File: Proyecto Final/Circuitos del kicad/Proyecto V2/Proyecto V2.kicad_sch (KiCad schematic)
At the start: 40 parts, among them J1 12v, J2 I2C + LCD, J3 DS1307, J4 Encoder, J5 Conn_01x02, J6 Conn_01x02, J7 Conn_01x02, J8 Conn_01x05, J9 Conn_01x05, K1 RAYEX-L90, K2 RAYEX-L90, K3 RAYEX-L90, Q1 PN2222A, Q2 PN2222A, Q3 PN2222A, SW1 SW_Push, SW2 SW_Push, SW3 SW_Push, SW4 SW_Push, U1 LM7805, U3 ATmega328P-P, U4 NodeMCU1.0(ESP-12E), Y1 16MHz

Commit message: SEXOOO
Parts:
- removed J4: Encoder, Connector_PinSocket_2.54mm:PinSocket_1x05_P2.54mm_Vertical, symbol Connector_Generic:Conn_01x05
- removed J9: Conn_01x05, Connector_PinHeader_2.54mm:PinHeader_1x05_P2.54mm_Vertical, symbol Connector_Generic:Conn_01x05
- added J4: Conn_02x06_Odd_Even, Connector_PinHeader_2.54mm:PinHeader_2x06_P2.54mm_Vertical, symbol Connector_Generic:Conn_02x06_Odd_Even
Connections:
- net +5V: now also J4.1 (Pin_1), J4.2 (Pin_2)
- net GND: now also J4.11 (Pin_11), J4.12 (Pin_12)
- net at U3.23 (PC0): now also J4.8 (Pin_8)
- net at U3.24 (PC1): now also J4.6 (Pin_6)
- net at U3.4 (PD2): now also J4.3 (Pin_3)
- net at U3.5 (PD3): now also J4.5 (Pin_5)
- net at U3.6 (PD4): now also J4.7 (Pin_7)
- net at U3.11 (PD5): now also J4.9 (Pin_9)
- net at U3.25 (PC2): now also J4.4 (Pin_4)
- no-connect marks 34 -> 33

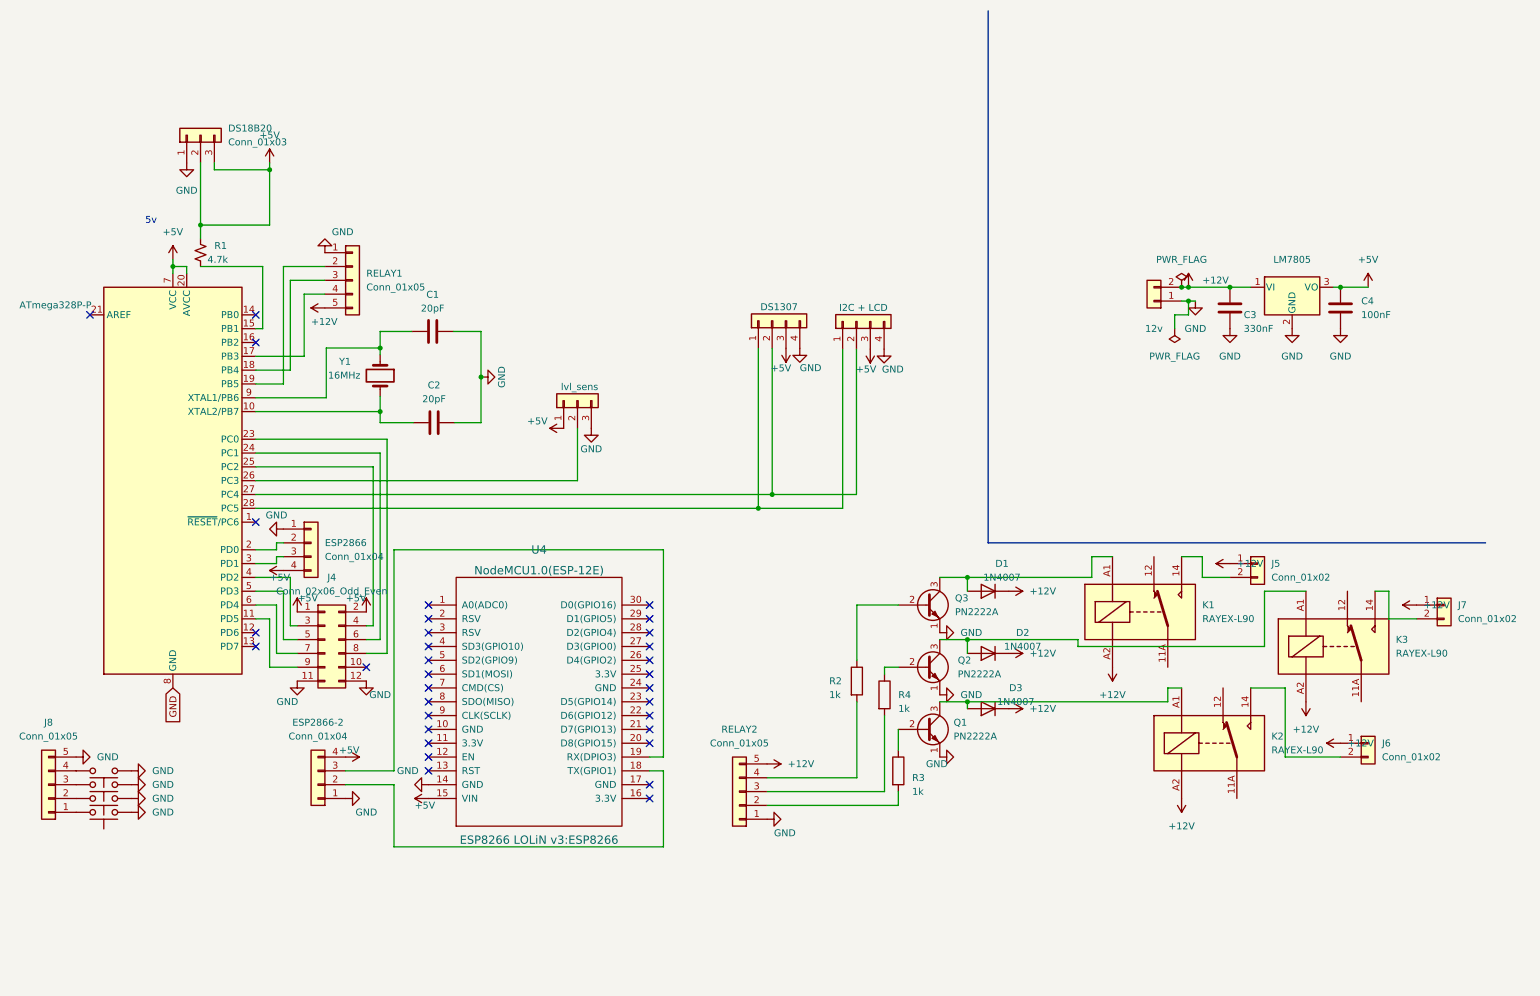
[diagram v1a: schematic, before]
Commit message: Resistencias pullup para pulsadores
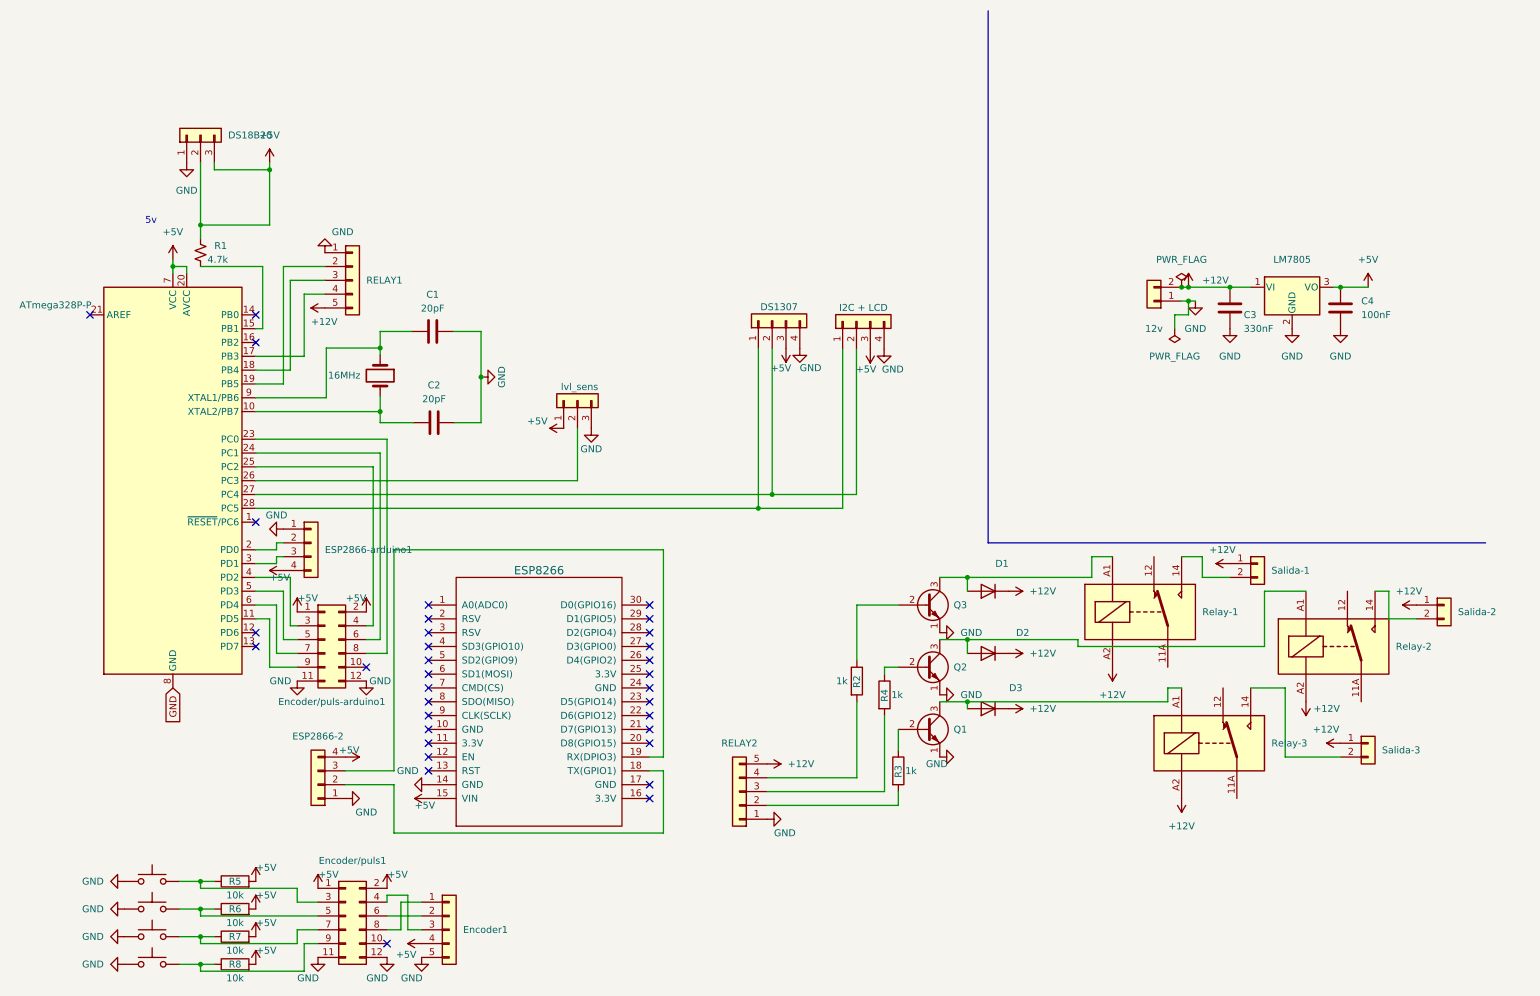
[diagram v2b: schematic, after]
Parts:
- removed J8: Conn_01x05, Connector_PinHeader_2.54mm:PinHeader_1x05_P2.54mm_Vertical, symbol Connector_Generic:Conn_01x05
- added Encoder/puls1: Conn_02x06_Odd_Even, Connector_PinHeader_2.54mm:PinHeader_2x06_P2.54mm_Vertical, symbol Connector_Generic:Conn_02x06_Odd_Even
- added Encoder1: Conn_01x05, Connector_PinSocket_2.54mm:PinSocket_1x05_P2.54mm_Vertical, symbol Connector_Generic:Conn_01x05
- added R5, R6, R7, R8: 10k, Resistor_THT:R_Axial_DIN0204_L3.6mm_D1.6mm_P5.08mm_Horizontal, symbol Device:R
- renumbered ESP2866 to ESP2866-arduino1, U4 to ESP8266, J4 to Encoder/puls-arduino1, K1 to Relay-1, K3 to Relay-2, K2 to Relay-3, J5 to Salida-1, J7 to Salida-2, J6 to Salida-3
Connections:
- net +5V: now also Encoder/puls1.1 (Pin_1), Encoder/puls1.2 (Pin_2), Encoder1.4 (Pin_4), R5.2, R6.2, R7.2, R8.2
- net GND: now also Encoder/puls1.11 (Pin_11), Encoder/puls1.12 (Pin_12), Encoder1.5 (Pin_5)
- net at SW2.2: now also Encoder/puls1.7 (Pin_7), R7.1
- net at SW3.2: now also Encoder/puls1.5 (Pin_5), R6.1
- net at SW1.2: now also Encoder/puls1.9 (Pin_9), R8.1
- net at SW4.2: now also Encoder/puls1.3 (Pin_3), R5.1
- new net: Encoder/puls1.4 (Pin_4), Encoder1.3 (Pin_3)
- new net: Encoder/puls1.6 (Pin_6), Encoder1.2 (Pin_2)
- new net: Encoder/puls1.8 (Pin_8), Encoder1.1 (Pin_1)
- no-connect marks 33 -> 34

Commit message: cambio bornera
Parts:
- Salida-1, Salida-2, Salida-3: footprint Connector_PinHeader_2.54mm:PinHeader_1x02_P2.54mm_Vertical -> TerminalBlock:TerminalBlock_bornier-2_P5.08mm
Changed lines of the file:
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@@
       (effects (font (size 1.27 1.27)) (justify left) hide)
     )
-    (property "Footprint" "Connector_PinHeader_2.54mm:PinHeader_1x02_P2.54mm_Vertical" (id 2) (at 264.16 146.05 0)
+    (property "Footprint" "TerminalBlock:TerminalBlock_bornier-2_P5.08mm" (id 2) (at 264.16 146.05 0)
       (effects (font (size 1.27 1.27)) hide)
     )
@@
       (effects (font (size 1.27 1.27)) (justify left) hide)
     )
-    (property "Footprint" "Connector_PinHeader_2.54mm:PinHeader_1x02_P2.54mm_Vertical" (id 2) (at 243.84 113.03 0)
+    (property "Footprint" "TerminalBlock:TerminalBlock_bornier-2_P5.08mm" (id 2) (at 243.84 113.03 0)
       (effects (font (size 1.27 1.27)) hide)
     )
@@
       (effects (font (size 1.27 1.27)) (justify left) hide)
     )
-    (property "Footprint" "Connector_PinHeader_2.54mm:PinHeader_1x02_P2.54mm_Vertical" (id 2) (at 278.13 120.65 0)
+    (property "Footprint" "TerminalBlock:TerminalBlock_bornier-2_P5.08mm" (id 2) (at 278.13 120.65 0)
       (effects (font (size 1.27 1.27)) hide)
     )
@@
     )
     (path "/1672224d-7982-4259-8536-1b27e643cf0c"
-      (reference "Salida-1") (unit 1) (value "Conn_01x02") (footprint "Connector_PinHeader_2.54mm:PinHeader_1x02_P2.54mm_Vertical")
+      (reference "Salida-1") (unit 1) (value "Conn_01x02") (footprint "TerminalBlock:TerminalBlock_bornier-2_P5.08mm")
     )
     (path "/2d58b5ac-6ee1-429c-aae4-017d7d7a7777"
-      (reference "Salida-2") (unit 1) (value "Conn_01x02") (footprint "Connector_PinHeader_2.54mm:PinHeader_1x02_P2.54mm_Vertical")
+      (reference "Salida-2") (unit 1) (value "Conn_01x02") (footprint "TerminalBlock:TerminalBlock_bornier-2_P5.08mm")
     )
     (path "/0e4578a7-20c6-4026-9829-3af9154dfc8a"
-      (reference "Salida-3") (unit 1) (value "Conn_01x02") (footprint "Connector_PinHeader_2.54mm:PinHeader_1x02_P2.54mm_Vertical")
+      (reference "Salida-3") (unit 1) (value "Conn_01x02") (footprint "TerminalBlock:TerminalBlock_bornier-2_P5.08mm")
     )
     (path "/5e9ee1d8-0d45-49f7-a578-4bbba6bc5d3c"
